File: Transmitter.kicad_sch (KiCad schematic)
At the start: 9 parts, among them J6 Terminal, U4 MAX485EE

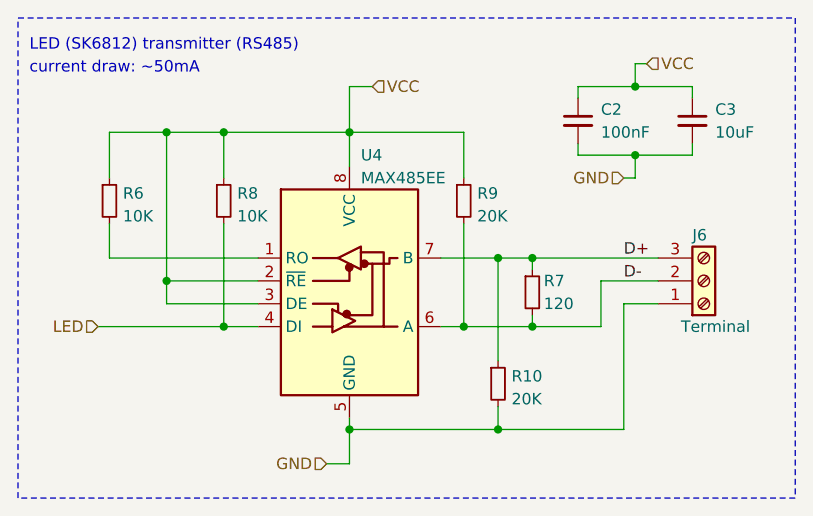
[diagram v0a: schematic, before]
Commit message: rename to v1 (to match silkscreen), improve readme and schematics layouts
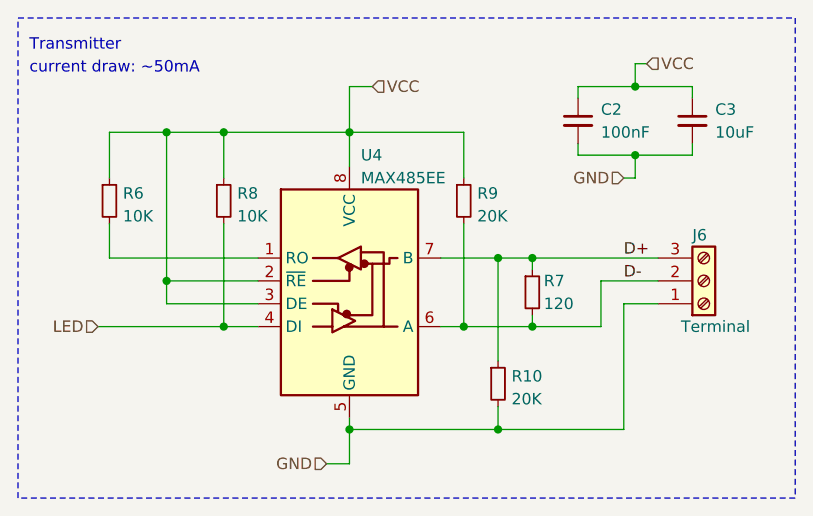
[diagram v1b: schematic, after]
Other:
- note added: "Transmitter"
- note removed: "LED (SK6812) transmitter (RS485)"
